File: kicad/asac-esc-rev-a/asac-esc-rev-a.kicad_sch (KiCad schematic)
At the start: 7 parts

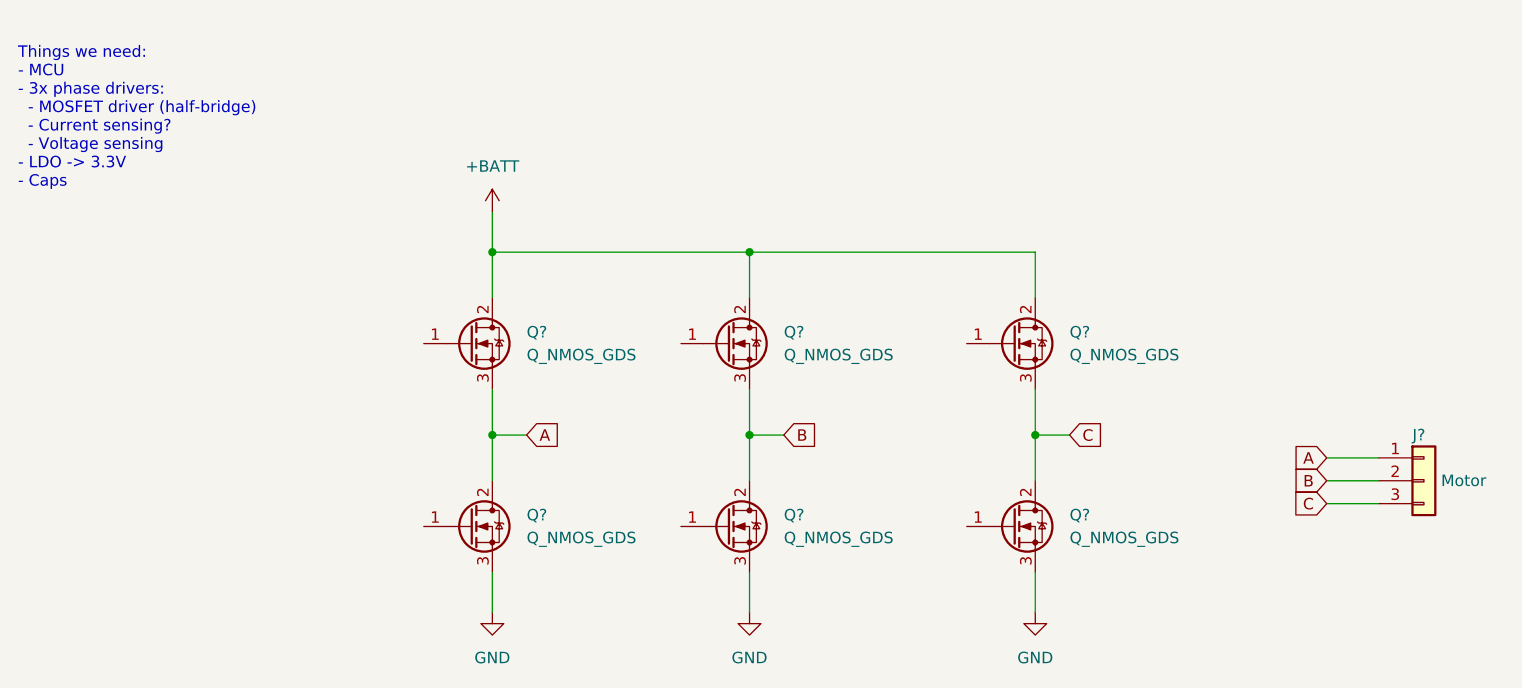
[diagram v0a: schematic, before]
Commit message: Created separate sheet for phase A, almost done with it.
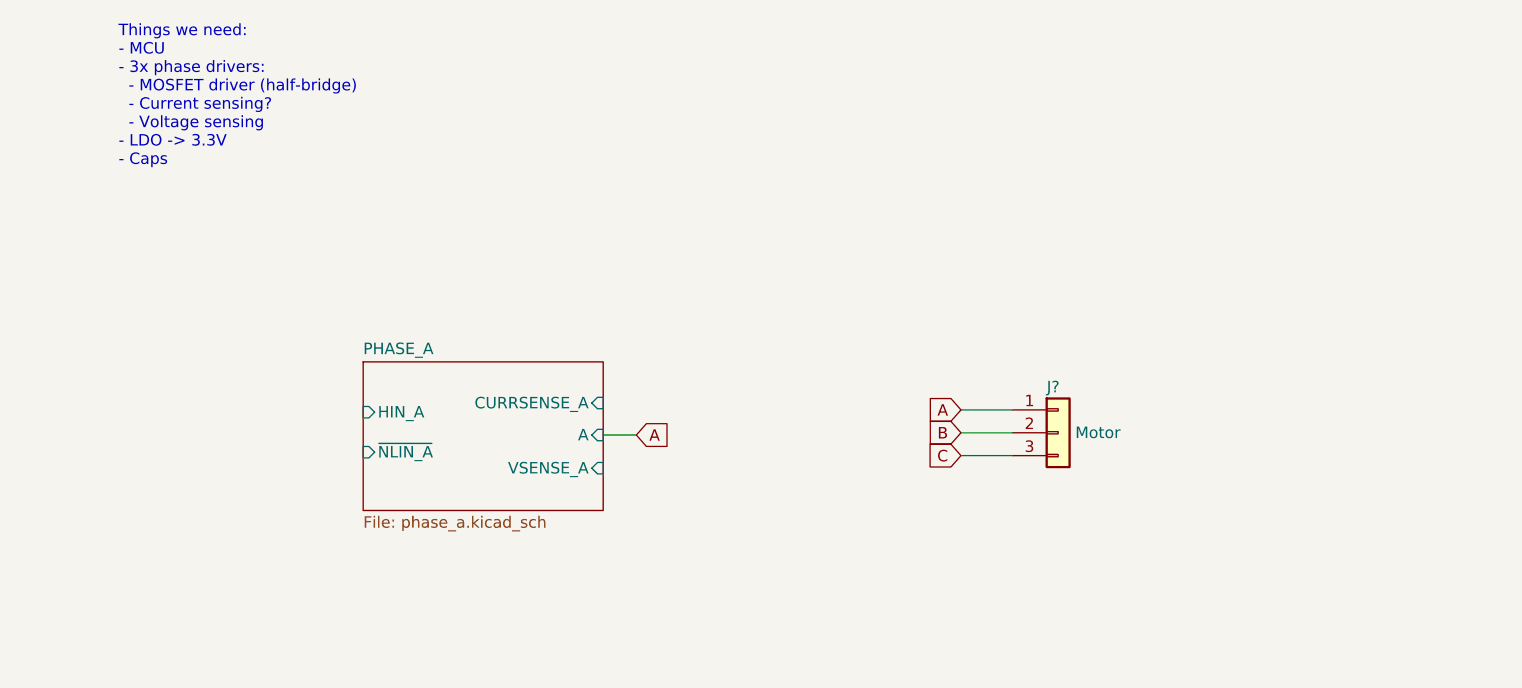
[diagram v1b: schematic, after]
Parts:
- removed Q? (x6): Q_NMOS_GDS, symbol Device:Q_NMOS_GDS
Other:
- added sheet PHASE_A (phase_a.kicad_sch)
- moved on the sheet: J?

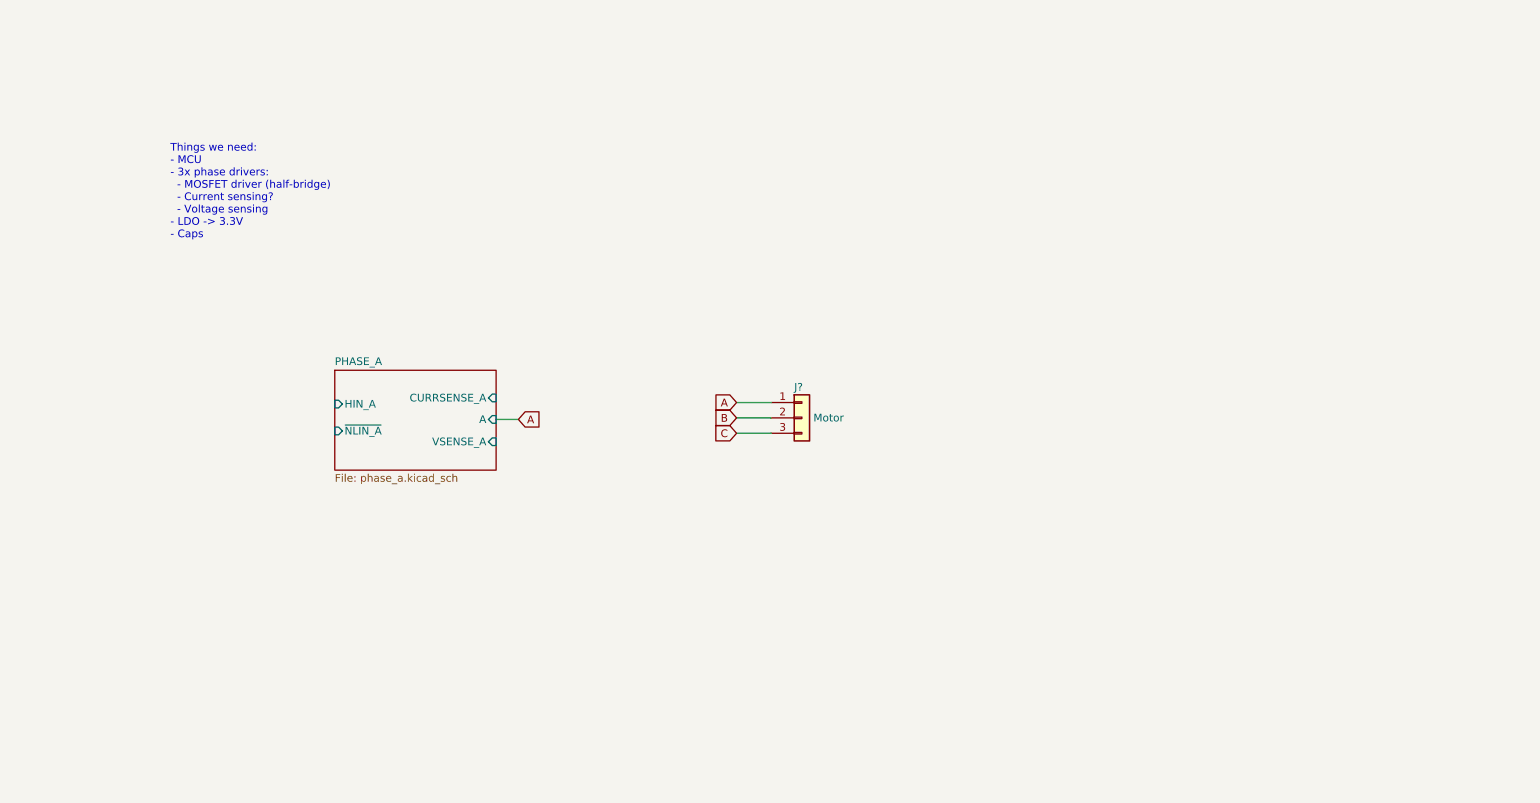
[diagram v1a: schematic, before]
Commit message: Decided on microcontroller: STM32C011F6P6. The reason for this mcu is that it's quite new, quite cheap, is available on LCSC is developed and maintained by STM. The mcu should have just enough pins for handling a single brushless motor.
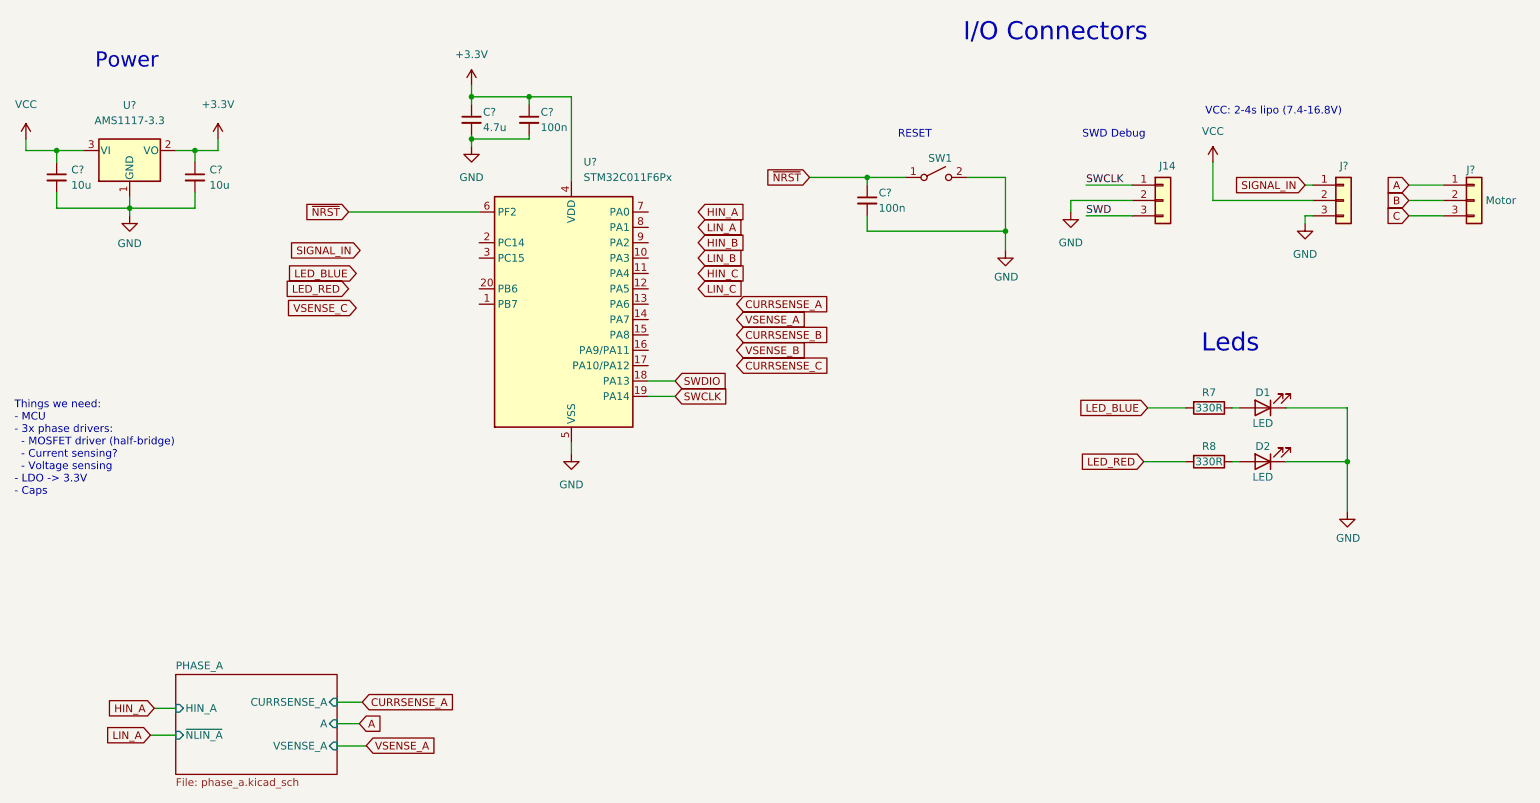
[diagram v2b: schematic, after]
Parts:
- added C? (x2): 100n, symbol Device:C_Small
- added C? (x2): 10u, symbol Device:C_Small
- added C?: 4.7u, symbol Device:C_Small
- added D1, D2: LED, Custom:LED_0603_no_outline, symbol Device:LED
- added J14, J?: Conn_01x03, Custom:PinHeader_1x03_P1.27mm_Vertical_no_silk_smd, symbol Connector_Generic:Conn_01x03
- added R7, R8: 330R, Resistor_SMD:R_0402_1005Metric, symbol Device:R
- added SW1: SW_SPST, Custom:SW-SMD_TS-1086EV-16, symbol Switch:SW_SPST
- added U?: STM32C011F6Px, Package_SO:TSSOP-20_4.4x6.5mm_P0.65mm, symbol MCU_ST_STM32C0:STM32C011F6Px
- added U?: AMS1117-3.3, Package_TO_SOT_SMD:SOT-223-3_TabPin2, symbol Regulator_Linear:AMS1117-3.3
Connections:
- new net: D1.2 (A), R7.1
- new net: D2.2 (A), R8.1
- new net +3.3V: C?.1, C?.1, C?.1, U?.2 (VO), U?.4 (VDD)
- new net GND: C?.2, C?.2, C?.2, C?.2, C?.2, D1.1 (K), D2.1 (K), J14.2 (Pin_2), J?.3 (Pin_3), SW1.2 (B), U?.1 (GND), U?.5 (VSS)
- new net LED_BLUE: R7.2
- new net LED_RED: R8.2
- new net SIGNAL_IN: J?.1 (Pin_1)
- new net SWCLK: J14.1 (Pin_1), U?.19 (PA14)
- new net SWD: J14.3 (Pin_3)
- new net SWDIO: U?.18 (PA13)
- new net VCC: C?.1, J?.2 (Pin_2), U?.3 (VI)
- new net ~{NRST}: C?.1, SW1.1 (A), U?.6 (PF2)
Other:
- note added: "I/O Connectors"
- note added: "Leds"
- note added: "Power"
- note added: "RESET"
- note added: "SWD Debug"
- note added: "VCC: 2-4s lipo (7.4-16.8V)"
- moved on the sheet: J?

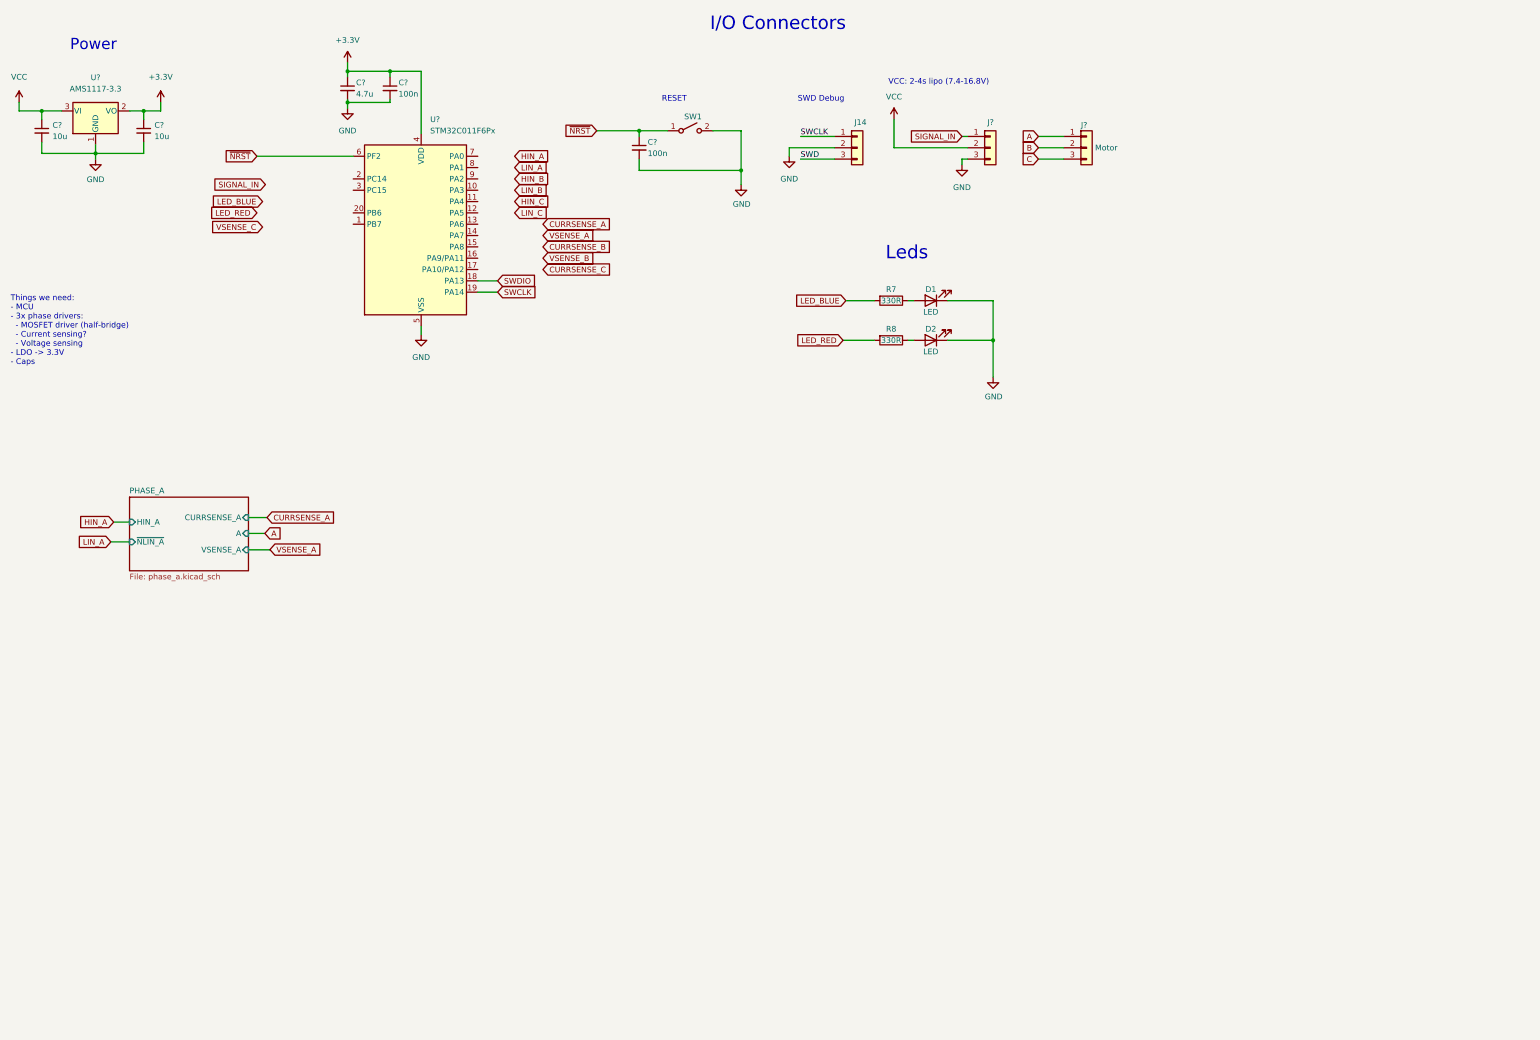
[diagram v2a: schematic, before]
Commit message: Changed from current sensing each phase to a single current sensing circuit for all MOSFETs. Primary motivation is that it's simpler, let's just hope that it works OK...!
Pretty much done with schematic now, everything is not
connected to the MCU yet however, since the layout might
have an impact on exactly which port should be connected
where.
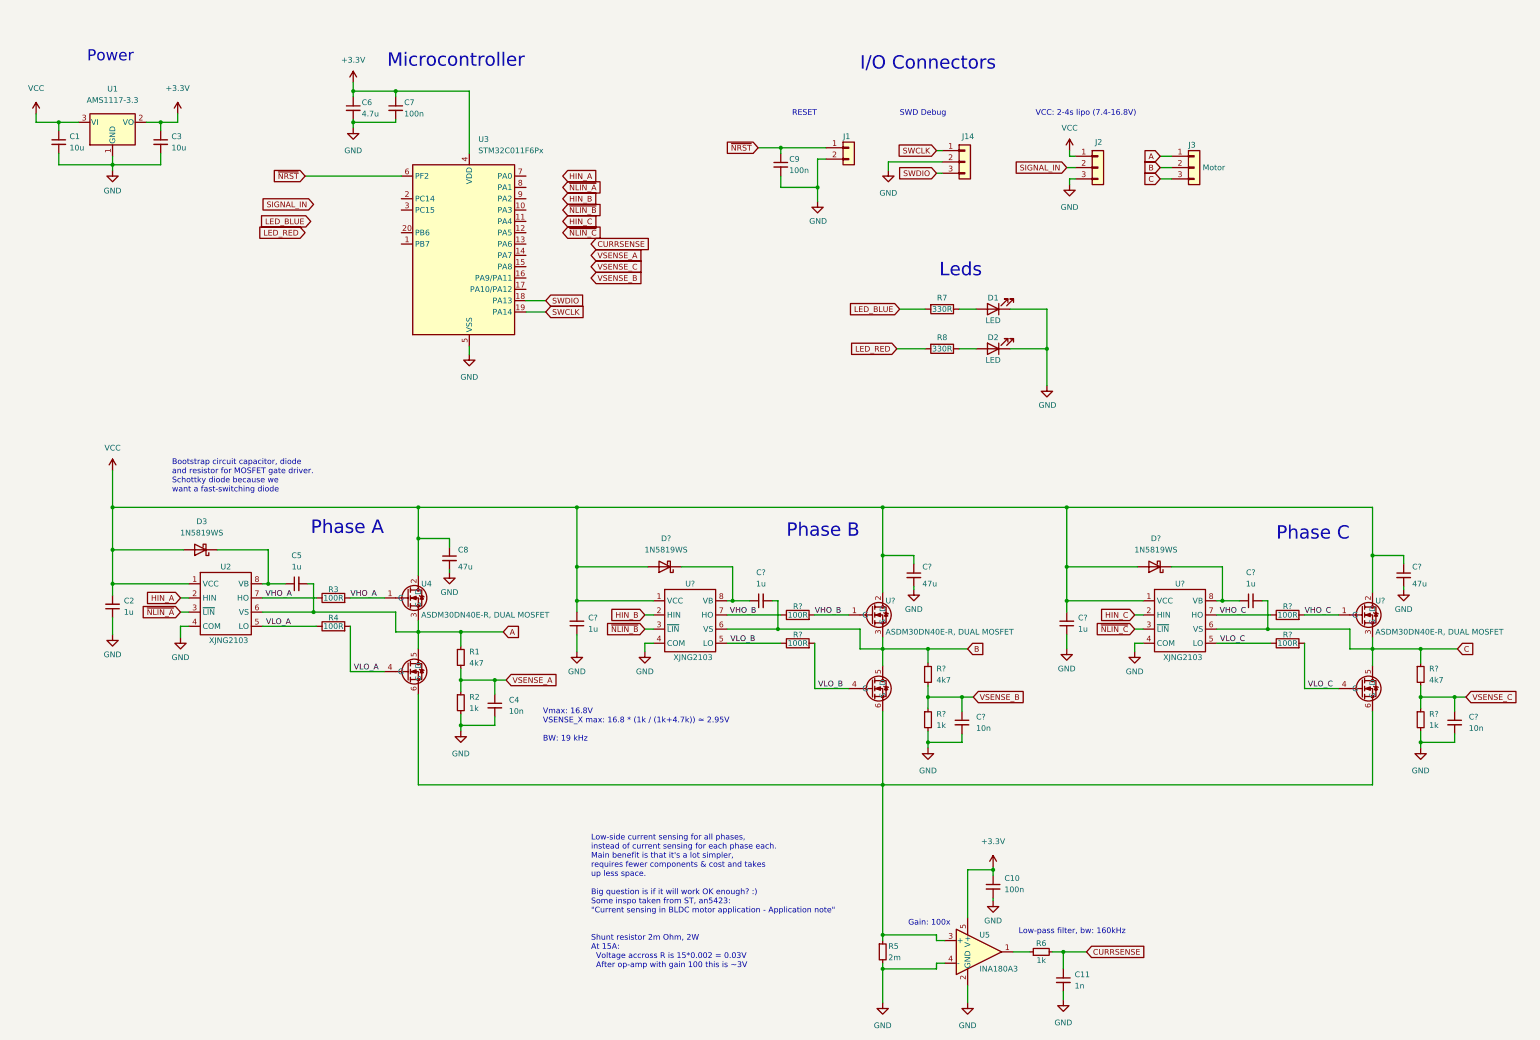
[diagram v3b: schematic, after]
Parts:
- removed SW1: SW_SPST, Custom:SW-SMD_TS-1086EV-16, symbol Switch:SW_SPST
- added C10: 100n, Capacitor_SMD:C_0402_1005Metric, symbol Device:C_Small
- added C11: 1n, Capacitor_SMD:C_0402_1005Metric, symbol Device:C_Small
- added C2, C5, C? (x4): 1u, Capacitor_SMD:C_0402_1005Metric, symbol Device:C_Small
- added C4, C? (x2): 10n, Capacitor_SMD:C_0402_1005Metric, symbol Device:C_Small
- added C8, C? (x2): 47u, Capacitor_SMD:C_1206_3216Metric, symbol Device:C_Small
- added D3, D? (x2): 1N5819WS, Diode_SMD:D_SOD-323, symbol Diode:1N5819WS
- added J1: Conn_01x02_RESET, Custom:PinHeader_1x02_P1.27mm_Vertical_No_Silk, symbol Connector_Generic:Conn_01x02
- added R1, R? (x2): 4k7, Resistor_SMD:R_0402_1005Metric, symbol Device:R_Small
- added R2, R6, R? (x2): 1k, Resistor_SMD:R_0402_1005Metric, symbol Device:R_Small
- added R3, R4, R? (x4): 100R, Resistor_SMD:R_0603_1608Metric, symbol Device:R
- added R5: 2m, Resistor_SMD:R_2512_6332Metric, symbol Device:R_Small
- added U2, U? (x2): XJNG2103, Package_SO:SOIC-8_3.9x4.9mm_P1.27mm, symbol Custom2:XJNG2103_MOSFET_GATE_DRIVER
- added U4, U? (x2): ASDM30DN40E-R, DUAL MOSFET, Custom:PDFN3333-8_L3.2-W3.1-P0.65-LS3.4-BL, symbol Custom2:ASDM30DN40E-R_MOSFET_DUAL
- added U5: INA180A3, Package_TO_SOT_SMD:SOT-23-5, symbol Amplifier_Current:INA180A3
- C1, C3: renamed from C?; footprint (none) -> Capacitor_SMD:C_0805_2012Metric
- C6: renamed from C?; footprint (none) -> Capacitor_SMD:C_0603_1608Metric
- C7, C9: renamed from C?; footprint (none) -> Capacitor_SMD:C_0402_1005Metric
- J2: renamed from J?; footprint Custom:PinHeader_1x03_P1.27mm_Vertical_no_silk_smd -> Custom:Conn_01x03_BLDC
- J3: renamed from J?; footprint (none) -> Custom:Conn_01x03_BLDC
- gave numbers to parts that had none: 2
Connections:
- net SWD is gone; now on net SWDIO: J14.3 (Pin_3)
- net +3.3V: now also C10.1, U5.5 (V+)
- net A: now also C5.2, R1.1, U2.6 (VS), U4.3 (S), U4.5 (D)
- net B: now also C?.2, R?.1, U?.3 (S), U?.5 (D), U?.6 (VS)
- net C: now also C?.2, R?.1, U?.3 (S), U?.5 (D), U?.6 (VS)
- net GND: now also C10.2, C11.2, C2.1, C4.2, C8.2, C?.1, C?.1, C?.2, C?.2, C?.2, C?.2, J1.2 (Pin_2), R2.2, R5.2, R?.2, R?.2, U2.4 (COM), U5.2 (GND), U5.4 (-), U?.4 (COM), U?.4 (COM)
- net HIN_A: now also U2.2 (HIN)
- net HIN_B: now also U?.2 (HIN)
- net HIN_C: now also U?.2 (HIN)
- net SIGNAL_IN: now also J2.2 (Pin_2); no longer J2.1 (Pin_1)
- net VCC: now also J2.1 (Pin_1), C2.2, C8.1, C?.1, C?.1, C?.2, C?.2, D3.2 (A), D?.2 (A), D?.2 (A), U2.1 (VCC), U4.2 (D), U?.1 (VCC), U?.1 (VCC), U?.2 (D), U?.2 (D); no longer J2.2 (Pin_2)
- net VSENSE_A: now also C4.1, R1.2, R2.1
- net VSENSE_B: now also C?.1, R?.1, R?.2
- net VSENSE_C: now also C?.1, R?.1, R?.2
- net ~{NRST}: now also J1.1 (Pin_1)
- new net: C?.1, D?.1 (K), U?.8 (VB) (x2)
- new net: R5.1, U4.6 (S), U5.3 (+), U?.6 (S), U?.6 (S)
- new net: C5.1, D3.1 (K), U2.8 (VB)
- new net: R6.1, U5.1
- new net CURRSENSE: C11.1, R6.2
- new net VHO_A: R3.1, R3.2, U2.7 (HO), U4.1 (G)
- new net VHO_B: R?.1, R?.2, U?.1 (G), U?.7 (HO)
- new net VHO_C: R?.1, R?.2, U?.1 (G), U?.7 (HO)
- new net VLO_A: R4.1, R4.2, U2.5 (LO), U4.4 (G)
- new net VLO_B: R?.1, R?.2, U?.4 (G), U?.5 (LO)
- new net VLO_C: R?.1, R?.2, U?.4 (G), U?.5 (LO)
- new net ~{NLIN_A}: U2.3 (~{LIN})
- new net ~{NLIN_B}: U?.3 (~{LIN})
- new net ~{NLIN_C}: U?.3 (~{LIN})
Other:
- removed sheet PHASE_A
- note added: "Bootstrap circuit capacitor, diode and resistor for MOSFET gate driver. Schottky diode because we want a fast-switching diode"
- note added: "Gain: 100x"
- note added: "Low-pass filter, bw: 160kHz"
- note added: "Low-side current sensing for all phases, instead of current sensing for each phase each. Main benefit is that it's a lot simpler, requires fewer components & cost and takes up less space. Big question is if it will work OK enough? :) Some inspo taken from ST, an5423: "Current sensing in BLDC motor application - Application note" Shunt resistor 2m Ohm, 2W At 15A: Voltage accross R is 15*0.002 = 0.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"
- note added: "Microcontroller"
- note added: "Phase A"
- note added: "Phase B"
- note added: "Phase C"
- note added: "Vmax: 16.8V VSENSE_X max: 16.8 * (1k / (1k+4.7k)) ≃ 2.95V BW: 19 kHz"
- note removed: "Things we need: - MCU - 3x phase drivers: - MOSFET driver (half-bridge) - Current sensing? - Voltage sensing - LDO -> 3.3V - Caps"
- company: (none) -> Victor Krook
- title: (none) -> ASAC ESC
- moved on the sheet: C1, C3, C6, C7, C9, D1, D2, J14, J2, J3, R7, R8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
